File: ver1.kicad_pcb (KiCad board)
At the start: 2 copper layers, 46 x 38 mm, 36 parts, among them P1 CONN_6, P2 CONN_2, P3 CONN_4, P4 CONN_4, P5 CONN_4, U1 MCP1790, U2 STM32F100C6, U3 DRV8833C, U4 DRV8833C, U5 DRV8833C

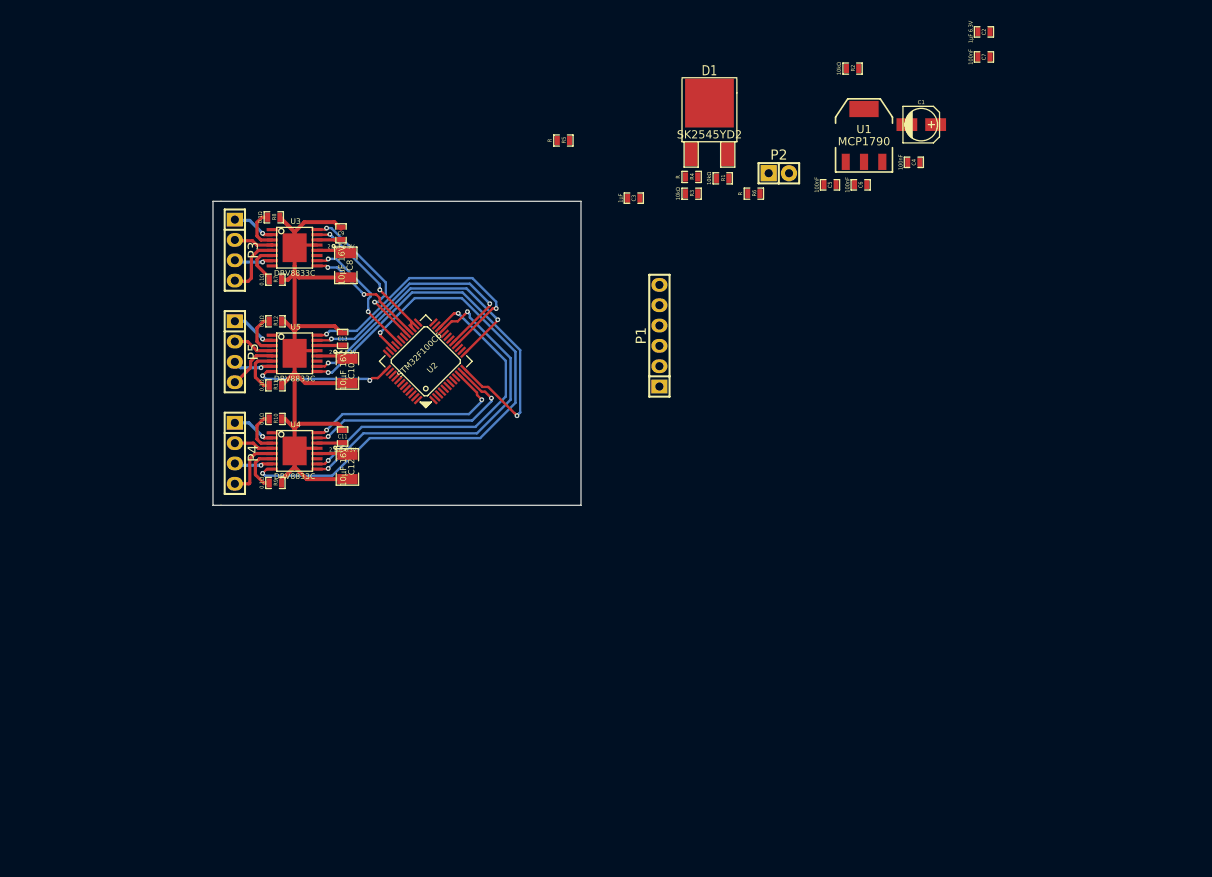
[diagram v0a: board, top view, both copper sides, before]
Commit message: Added footprints, checking in before redoing routing
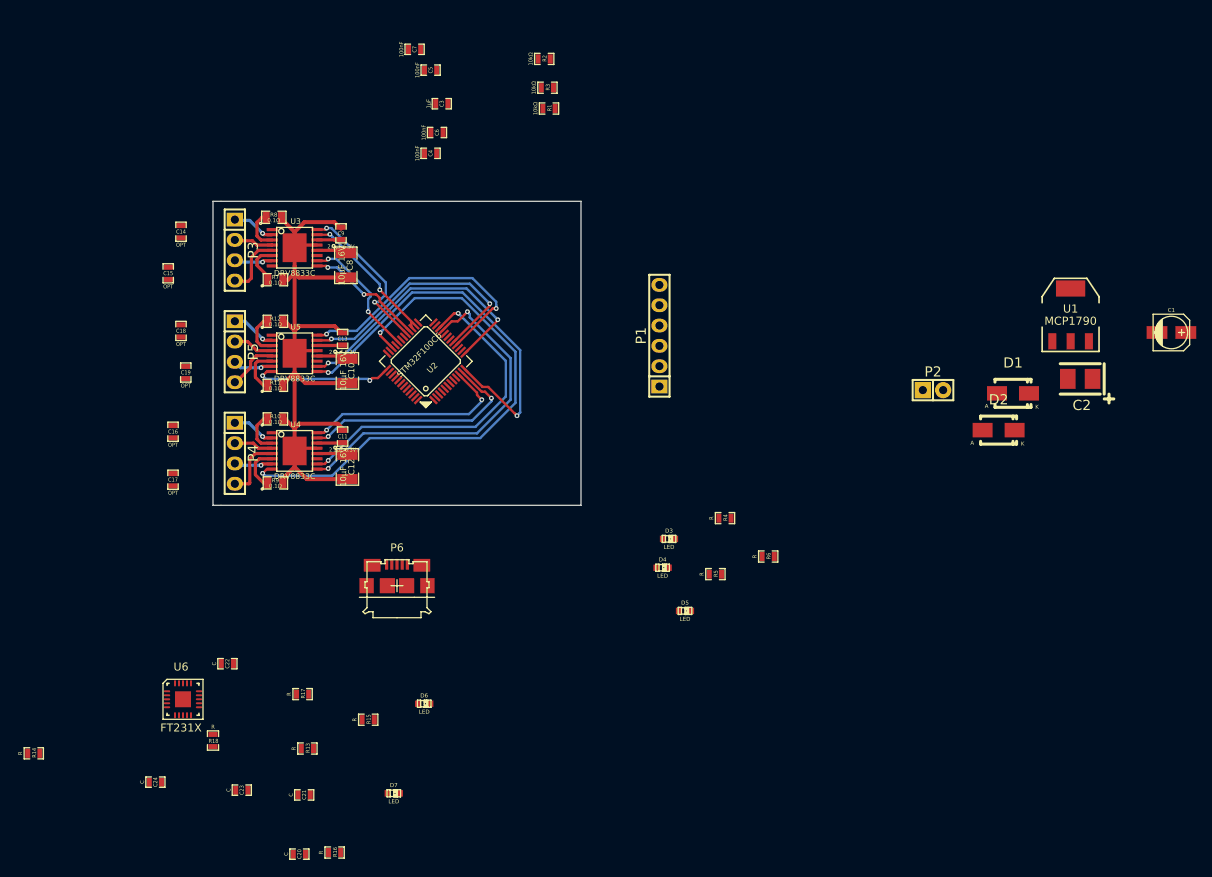
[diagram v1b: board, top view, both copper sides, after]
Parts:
- added C14: OPT, SMD_Packages:SMD-0603_c, F.Cu at (86.0, 90.8)
- added C15: OPT, SMD_Packages:SMD-0603_c, F.Cu at (84.4, 96.0)
- added C16: OPT, SMD_Packages:SMD-0603_c, F.Cu at (85.0, 115.8)
- added C17: OPT, SMD_Packages:SMD-0603_c, F.Cu at (85.0, 121.8)
- added C18: OPT, SMD_Packages:SMD-0603_c, F.Cu at (86.0, 103.2)
- added C19: OPT, SMD_Packages:SMD-0603_c, F.Cu at (86.6, 108.4)
- added C20: C, SMD_Packages:SMD-0603_c, F.Cu at (100.8, 168.6)
- added C21: C, SMD_Packages:SMD-0603_c, F.Cu at (101.4, 161.2)
- added C22: C, SMD_Packages:SMD-0603_c, F.Cu at (91.8, 144.8)
- added C23: C, SMD_Packages:SMD-0603_c, F.Cu at (93.6, 160.6)
- added C24: C, SMD_Packages:SMD-0603_c, F.Cu at (82.8, 159.6)
- added D2: DIODESCH, Diodes_SMD:Diode-SMA_Standard, F.Cu at (188.2, 115.6)
- added D3: LED, LEDs:LED-0603, F.Cu at (147.0, 129.2)
- added D4: LED, LEDs:LED-0603, F.Cu at (146.2, 132.8)
- added D5: LED, LEDs:LED-0603, F.Cu at (149.0, 138.2)
- added D6: LED, LEDs:LED-0603, F.Cu at (116.4, 149.8)
- added D7: LED, LEDs:LED-0603, F.Cu at (112.6, 161.0)
- added P6: USB_Micro_B, micro_usb_b:USB MICRO B, F.Cu at (113.0, 135.1)
- added R13: R, SMD_Packages:SMD-0603_r, F.Cu at (101.8, 155.4)
- added R14: R, SMD_Packages:SMD-0603_r, F.Cu at (67.6, 156.0)
- added R15: R, SMD_Packages:SMD-0603_r, F.Cu at (109.4, 151.8)
- added R16: R, SMD_Packages:SMD-0603_r, F.Cu at (105.2, 168.4)
- added R17: R, SMD_Packages:SMD-0603_r, F.Cu at (101.2, 148.6)
- added R18: R, SMD_Packages:SMD-0603_r, F.Cu at (90.0, 154.4)
- added U6: FT231X, qfn20:QFN_20-1EP, F.Cu at (86.0, 149.0)
- C2: footprint SMD_Packages:SMD-0603_c -> Capacitors_Tantalum_SMD:TantalC_SizeB_EIA-3528_Reflow
- D1: value SK2545YD2 -> DIODESCH; footprint SMD_Packages:DPAK-2 -> Diodes_SMD:Diode-SMA_Standard
- R10, R11, R12, R7, R8, R9: footprint SMD_Packages:SMD-0603_r -> SMD_Packages:SMD-0805
- moved C7 71.2 mm to (115.2, 68.0)
- moved C4 60.4 mm to (117.2, 81.0)
- moved R5 57.4 mm to (152.8, 133.6)
- moved C6 53.4 mm to (118.0, 78.4)
- moved C5 51.9 mm to (117.2, 70.6)
- moved D1 48.3 mm to (190.0, 111.0)
- moved R6 45.4 mm to (159.4, 131.4)
- moved C2 45.0 mm to (198.4, 109.2), turned to 180 degrees
- moved R4 42.9 mm to (154.0, 126.6)
- moved C1 40.7 mm to (209.8, 103.4)
- moved R2 38.6 mm to (131.4, 69.2)
- moved U1 34.2 mm to (197.2, 101.2)
- moved P2 33.3 mm to (180.0, 110.6)
- moved C3 26.7 mm to (118.6, 74.8)
- moved R1 23.4 mm to (132.0, 75.4)
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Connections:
- net /BOOT0 renamed /PC Interface/DTR
- net /MCU_RX renamed /PC Interface/TX
- net /MCU_TX renamed /PC Interface/RX
- net /NRST renamed /PC Interface/RTS
- C1 pad 1: VDD -> Net-(C1-Pad1)
- D1 pad 1: GND -> VDD
- D1 pad 2: VDD -> Net-(C1-Pad1)
- R4 pad 1: VCC -> Net-(D3-Pad2)
- R5 pad 1: VCC -> Net-(D4-Pad2)
- R6 pad 1: VCC -> Net-(D5-Pad2)
- U1 pad 1: VDD -> Net-(C1-Pad1)
- U2 pad 12: /drv8833_3/BIN1 -> (no net)
- U2 pad 13: /drv8833_3/BIN2 -> (no net)
- U2 pad 18: (no net) -> /drv8833_3/BIN1
- U2 pad 19: (no net) -> /drv8833_3/BIN2

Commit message: Tried a new layout for motor driver output
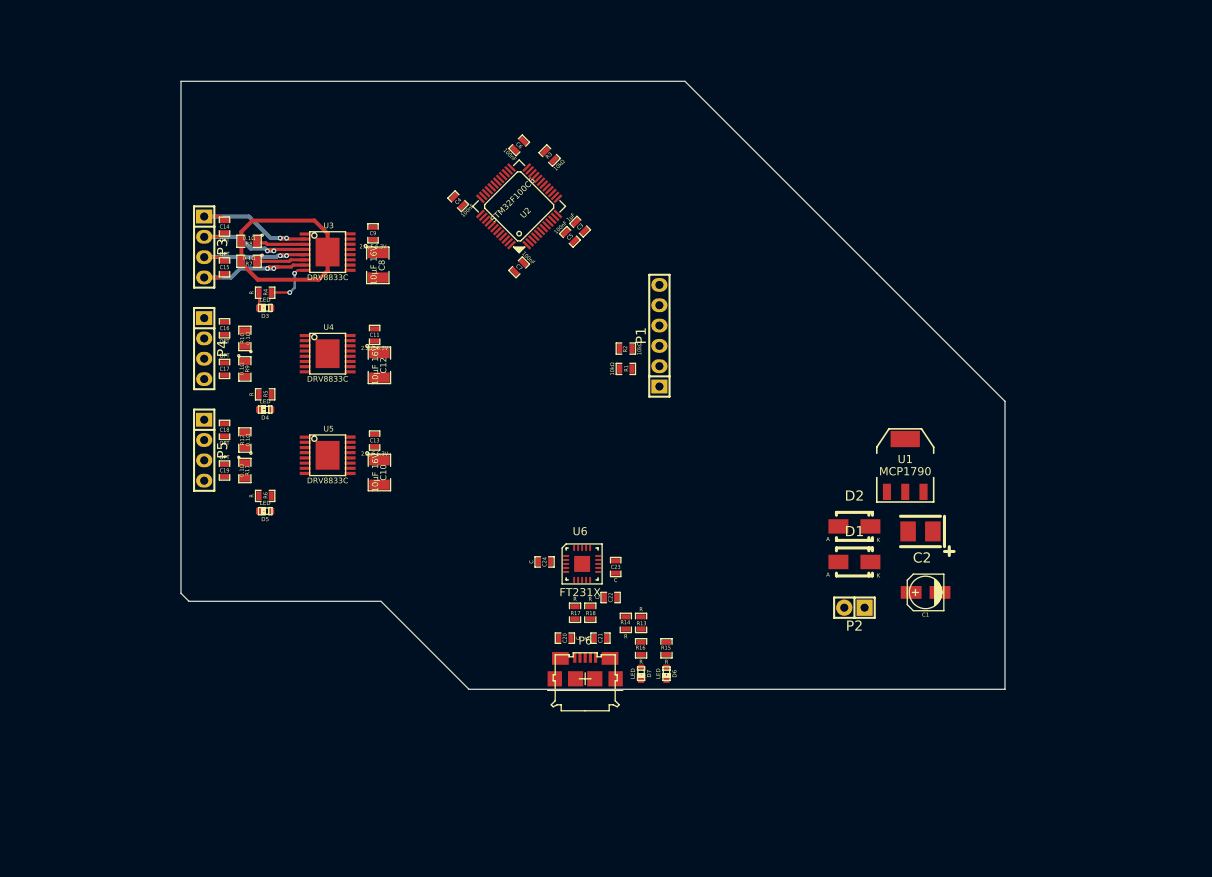
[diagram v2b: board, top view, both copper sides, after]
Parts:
- moved R14 75.8 mm to (141.6, 139.7), turned to 90 degrees
- moved R4 64.0 mm to (96.5, 98.4)
- moved R6 63.3 mm to (96.5, 123.8)
- moved R5 60.6 mm to (96.5, 111.1)
- moved D3 58.2 mm to (96.5, 100.3), turned to 180 degrees
- moved C24 55.9 mm to (131.4, 132.1)
- moved C23 54.4 mm to (140.3, 132.7), turned to 90 degrees
- moved D5 53.9 mm to (96.5, 125.7), turned to 180 degrees
- moved D4 53.5 mm to (96.5, 113.0), turned to 180 degrees
- moved U6 52.7 mm to (135.9, 132.1)
- moved R18 49.8 mm to (137.2, 138.4)
- moved C22 48.6 mm to (139.7, 136.5)
- moved R16 46.0 mm to (143.5, 142.9), turned to 90 degrees
- moved C1 44.7 mm to (179.1, 135.9), turned to 180 degrees
- moved R13 44.6 mm to (143.5, 139.7), turned to 270 degrees
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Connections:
- P3 pad 3: /drv8833_1/BOUT1 -> /drv8833_1/BOUT2
- P3 pad 4: /drv8833_1/BOUT2 -> /drv8833_1/BOUT1
- P4 pad 3: /drv8833_2/BOUT1 -> /drv8833_2/BOUT2
- P4 pad 4: /drv8833_2/BOUT2 -> /drv8833_2/BOUT1
- P5 pad 3: /drv8833_3/BOUT1 -> /drv8833_3/BOUT2
- P5 pad 4: /drv8833_3/BOUT2 -> /drv8833_3/BOUT1
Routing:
- net /drv8833_2/FAULT_OUT: track 67.3 -> 0.00 mm, vias 2 -> 0
- net GND: track 93.1 -> 32.7 mm
- net /drv8833_3/BIN1: track 49.9 -> 0.00 mm, vias 2 -> 0
- net /drv8833_2/BIN1: track 45.2 -> 0.00 mm, vias 2 -> 0
- net /drv8833_2/BIN2: track 43.5 -> 0.00 mm, vias 2 -> 0
- net /drv8833_3/AIN1: track 34.3 -> 0.00 mm, vias 2 -> 0
- net /drv8833_3/BIN2: track 34.2 -> 0.00 mm, vias 2 -> 0
- net /drv8833_3/AIN2: track 32.3 -> 0.00 mm, vias 2 -> 0
- net /drv8833_2/AIN2: track 29.0 -> 0.00 mm, vias 2 -> 0
- net /drv8833_2/AIN1: track 26.8 -> 0.00 mm, vias 2 -> 0
- net /drv8833_1/AIN1: track 20.5 -> 0.00 mm, vias 2 -> 0
- net /drv8833_3/FAULT_OUT: track 17.8 -> 0.00 mm, vias 2 -> 0
- net /drv8833_1/AIN2: track 17.7 -> 0.00 mm, vias 2 -> 0
- net /drv8833_1/BIN2: track 16.4 -> 0.00 mm, vias 2 -> 0
- net /drv8833_1/BIN1: track 15.2 -> 0.00 mm, vias 2 -> 0
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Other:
- board size 46 x 38 mm -> 103 x 76 mm

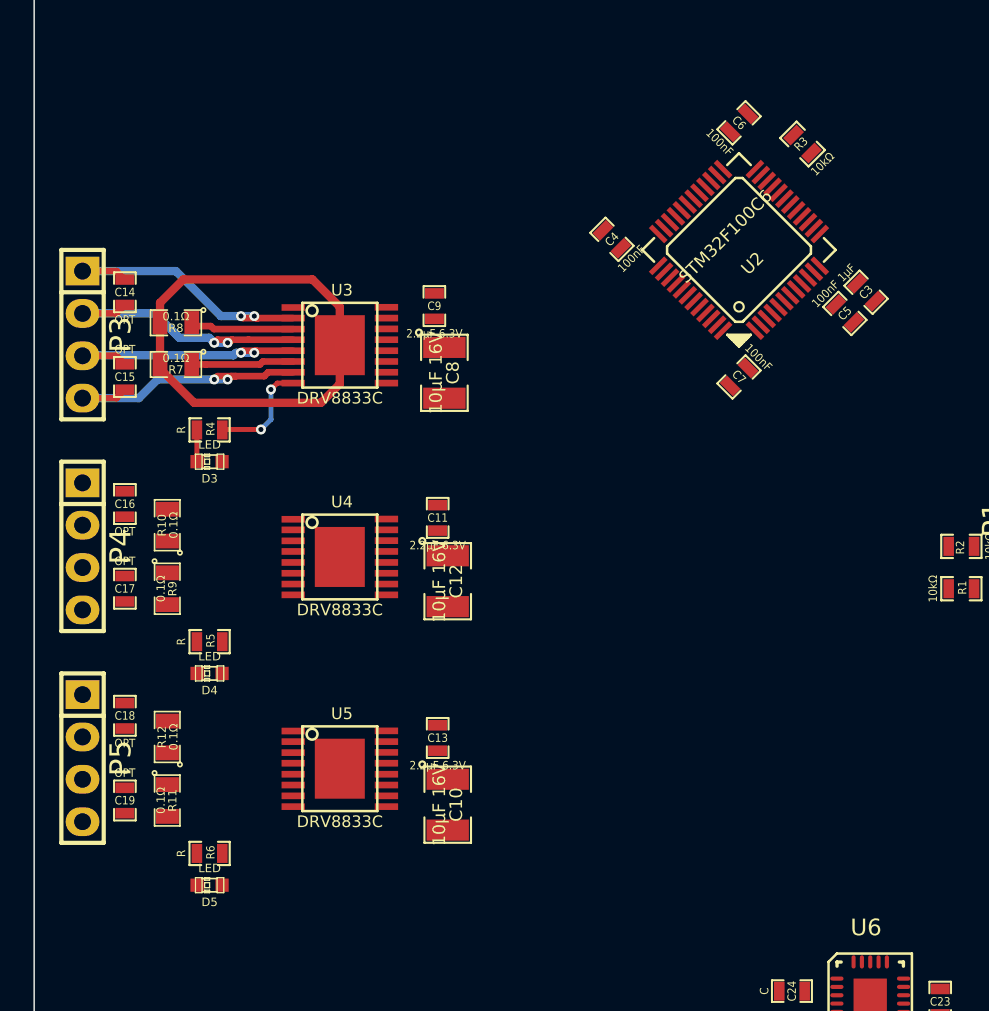
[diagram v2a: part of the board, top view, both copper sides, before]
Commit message: Rerouted motor output
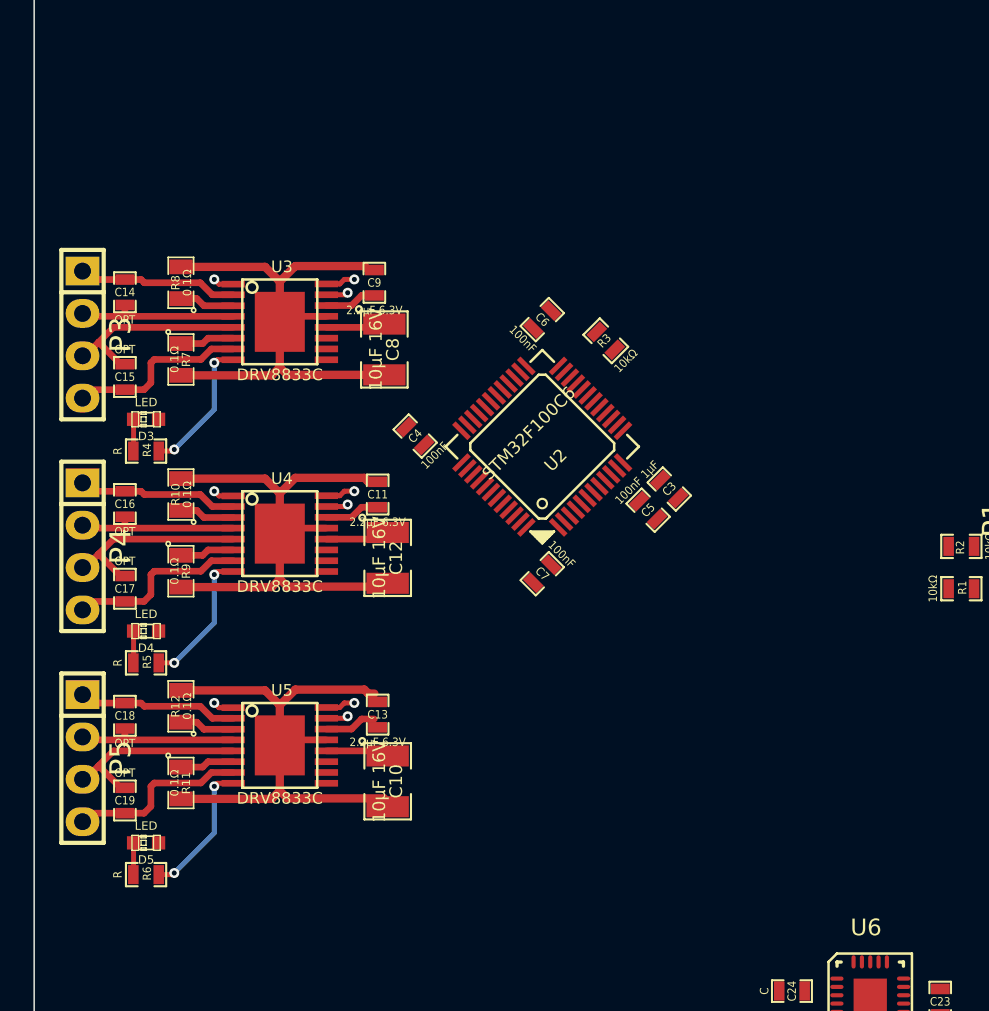
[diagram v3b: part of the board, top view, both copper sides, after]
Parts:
- moved U2 16.7 mm to (116.5, 99.4)
- moved C4 16.7 mm to (108.8, 98.8)
- moved C5 16.7 mm to (122.8, 103.2)
- moved C6 16.7 mm to (116.5, 91.8)
- moved C7 16.7 mm to (116.5, 107.0)
- moved R3 16.7 mm to (120.3, 93.1)
- moved C3 16.7 mm to (124.1, 102.0)
- moved D4 4.58 mm to (92.7, 110.5)
- moved D5 4.58 mm to (92.7, 123.2)
- moved D3 4.58 mm to (92.7, 97.8)
- moved R4 4.02 mm to (92.7, 99.7)
- moved R5 4.02 mm to (92.7, 112.4)
- moved R6 4.02 mm to (92.7, 125.1)
- moved C11 3.86 mm to (106.6, 102.3)
- moved C13 3.86 mm to (106.6, 115.5)
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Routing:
- net GND: track 32.7 -> 99.3 mm
- net /drv8833_2/BOUT2: track 0.00 -> 12.3 mm
- net /drv8833_3/BOUT2: track 0.00 -> 12.3 mm
- net /drv8833_3/BOUT1: track 0.00 -> 11.0 mm
- net /drv8833_2/BOUT1: track 0.00 -> 11.0 mm
- net /drv8833_3/AOUT2: track 0.00 -> 10.7 mm
- net /drv8833_2/AOUT2: track 0.00 -> 10.7 mm
- net VDD: track 0.00 -> 10.7 mm
- net /drv8833_2/AOUT1: track 0.00 -> 9.62 mm
- net /drv8833_3/AOUT1: track 0.00 -> 9.62 mm
- net /drv8833_2/FAULT_OUT: track 0.00 -> 8.44 mm, vias 0 -> 2
- net /drv8833_3/FAULT_OUT: track 0.00 -> 8.37 mm, vias 0 -> 2
- net /drv8833_1/AOUT1: track 17.6 -> 9.62 mm, vias 2 -> 0
- net /drv8833_1/AOUT2: track 17.3 -> 10.7 mm, vias 2 -> 0
- net /drv8833_1/BOUT1: track 17.4 -> 11.0 mm, vias 2 -> 0
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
